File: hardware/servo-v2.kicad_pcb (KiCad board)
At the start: 4 copper layers, 40 x 40 mm, 48 parts, among them P1 CON-SENSOR2, P2 BOOT, P3 DEBUG, P4 black, Q1 FDS8449, U1 XMC1404, U2 DRILL, U3 DRILL, U4 DRILL, U5 DRILL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

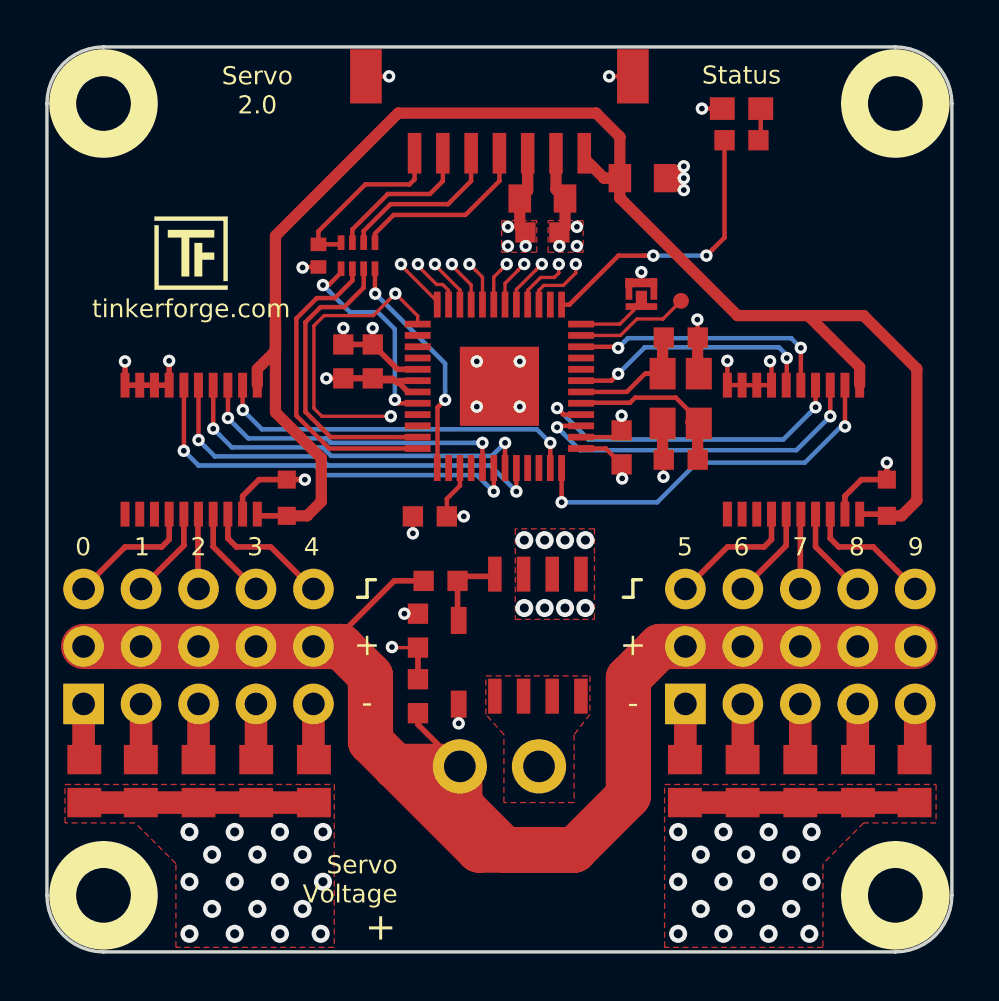
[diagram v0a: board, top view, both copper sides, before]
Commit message: New standart layout. Switched to Kicad 6
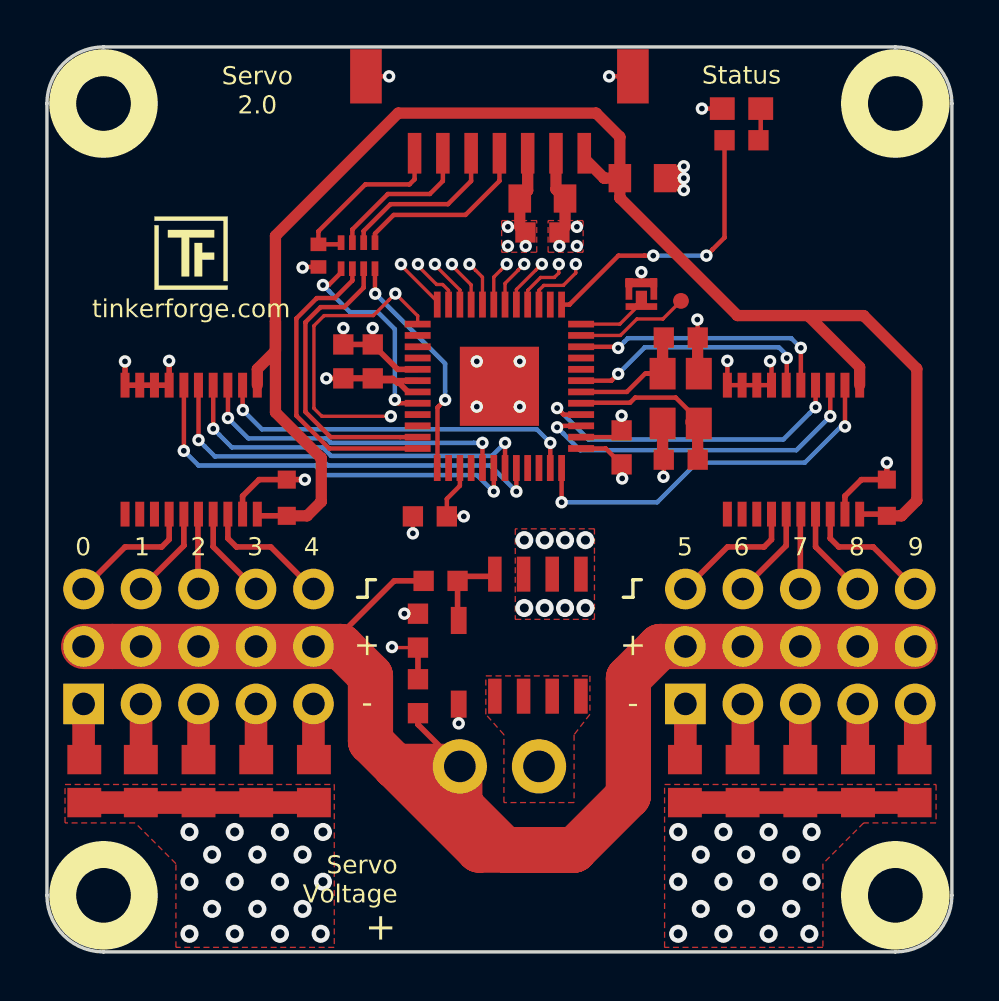
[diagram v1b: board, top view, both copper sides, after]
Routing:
- added copper zone on In1.Cu, net GND
- added copper zone on In2.Cu, net VCC
- removed copper zone on GND, net GND
- removed copper zone on VCC, net VCC
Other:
- net class Default removed

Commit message: Data Cleanup
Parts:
- moved G*** 0.08 mm to (136.4, 91.7)
- moved P2 0.08 mm to (156.3, 93.5)
- moved C10 0.08 mm to (140.6, 102.5)
- moved R12 0.07 mm to (160.8, 114.9)
- moved R5 0.07 mm to (139.3, 114.9)
- moved R7 0.07 mm to (134.1, 114.9)
- moved R9 0.07 mm to (168.4, 114.9)
- moved R10 0.07 mm to (165.8, 114.9)
- moved R8 0.07 mm to (131.7, 114.9)
- moved C9 0.06 mm to (158.0, 95.4)
- moved RP1 0.06 mm to (143.8, 91.7)
- moved C5 0.06 mm to (146.9, 103.2)
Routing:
- net V-EXT: track 25.9 -> 24.9 mm, vias 3 -> 2
